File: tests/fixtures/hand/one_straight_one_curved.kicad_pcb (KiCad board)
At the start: 2 copper layers, 20 x 12 mm, 0 parts

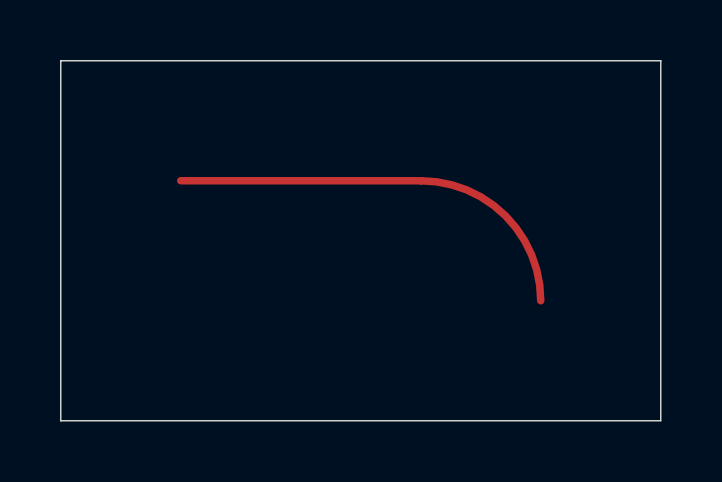
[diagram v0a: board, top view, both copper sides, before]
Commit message: fix(router): a via that came out of a file is not the router's to delete
The deletion filter asked !via.locked with no question about who put the via
there, so every via a person placed was removed on the next route - and nothing
on the import path could set a lock to save one.

The obvious fix was the wrong one. A trace has an author in a strong sense: its
shape is a decision, and TraceSource answers who drew it. A via is usually a
consequence of a decision, and a via imported from somebody else's autorouter
has no author this model could name - calling it Manual to keep it would be
false in the letter and right only in effect, and a field read against its own
name rots at the third reader.

What the filter needs is narrower and has a stable answer: did this router lay
this down, in this pass. RouterPlaced records exactly that. It is a component
rather than a field, and Stitched is the same shape for a different producer -
a via the stitcher generated from a rule - so this is a second marker of a kind
the model already has, not a new idea in it. It is attached only when
apply_routes_as is called with Autorouted, so an import materialising the file's
copper never carries it.

Provenance goes before reading (locked) from the file, decided on the cost of
being wrong. If the token turns out wrong and we had gone by the token,
imported vias keep vanishing silently, because a missing token reads exactly
like an absent lock. If the token turns out wrong and we go by provenance,
nothing happens. The two are different sentences and a board needs both - a
lock says do not touch this ever, provenance says do not delete this, it is not
yours - but most boards lock nothing, so a defence built on locks protects only
the people who already knew to defend themselves.

Verified:
  cargo test -p cypcb-kicad --test hand_drawn_copper_is_not_the_routers
    -> 5 passed; "1 via(s) from the file, 1 after a routing pass" and
       "1 via(s) the router placed, 0 after a routing pass"
  mu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
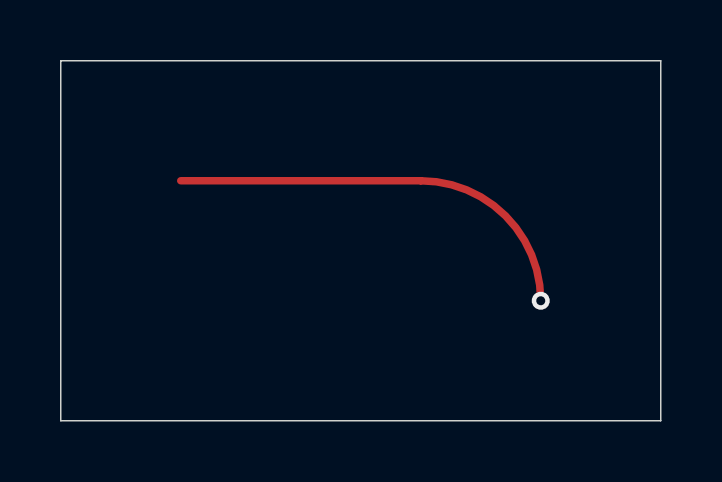
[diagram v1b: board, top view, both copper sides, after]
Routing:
- net HAND: vias 0 -> 1
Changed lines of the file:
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@@
   (segment (start 104.0 104.0) (end 112.0 104.0) (width 0.25) (layer "F.Cu") (net 1))
   (arc (start 112.0 104.0) (mid 114.828427 105.171573) (end 116.0 108.0) (width 0.25) (layer "F.Cu") (net 1))
+  (via (at 116.0 108.0) (size 0.6) (drill 0.3) (layers "F.Cu" "B.Cu") (net 1))
 )
